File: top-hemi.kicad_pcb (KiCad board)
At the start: 2 copper layers, 46 x 39 mm, 37 parts, among them J1 USB_B_Mini, J2 TC2030_NL, J3 FFC-0.5MM-6POS, J4 Port_1, J5 Port_2, J6 FFC-0.5MM-6POS, J7 Port_3, J8 Port_4, U1 PMIC-LDO-XC6204B332MR_SOT23-5_, U2 LP2985-5.0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

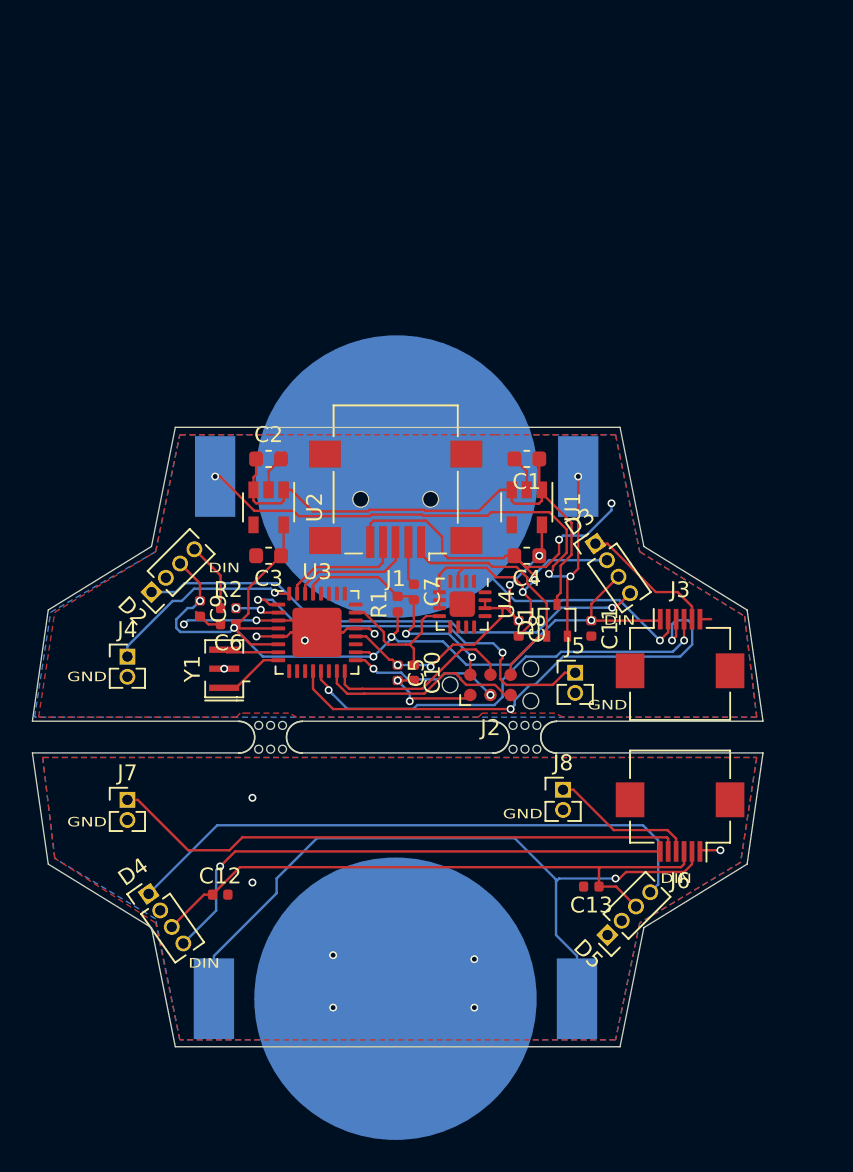
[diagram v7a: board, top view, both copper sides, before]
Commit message: Changed to 2.54mm
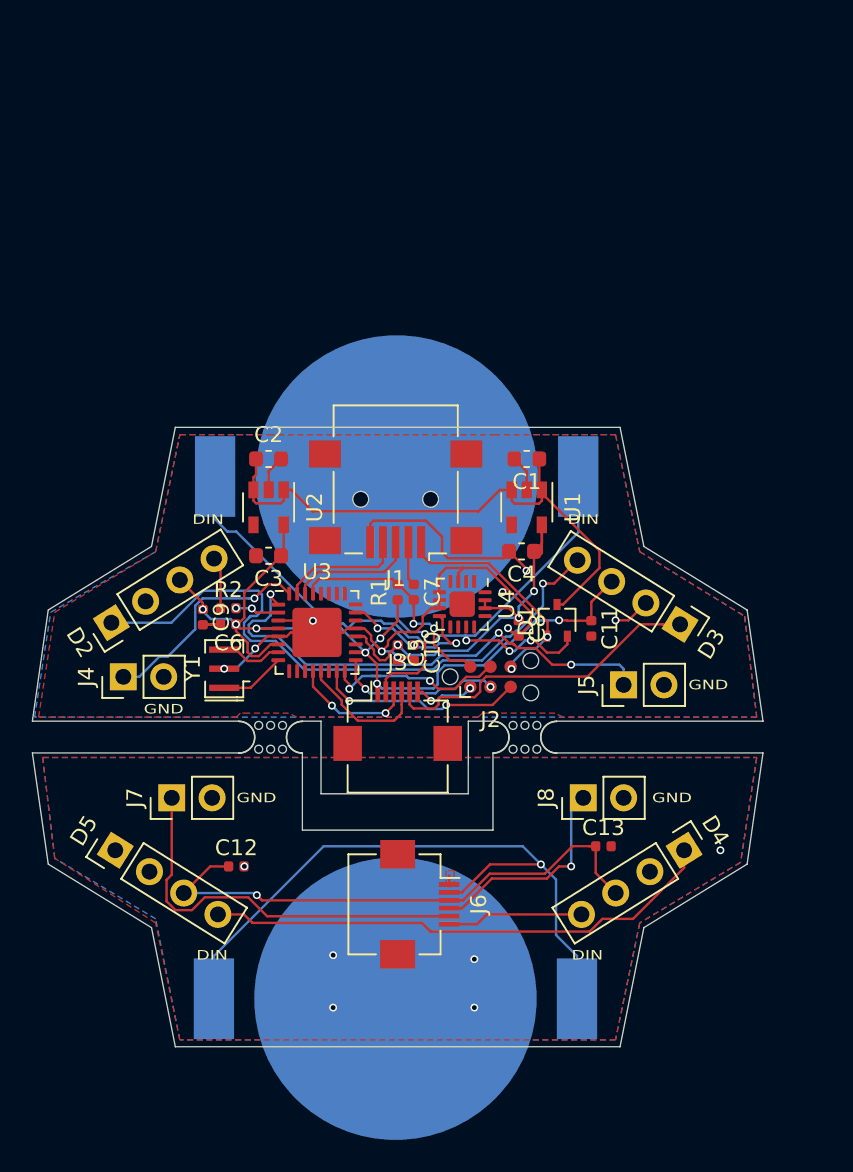
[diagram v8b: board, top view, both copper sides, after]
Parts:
- D2, D3, D4, D5: footprint Connector_PinHeader_1.27mm:PinHeader_1x04_P1.27mm_Vertical -> Connector_PinHeader_2.54mm:PinHeader_1x04_P2.54mm_Vertical
- J4, J5, J7, J8: footprint Connector_PinHeader_1.27mm:PinHeader_1x02_P1.27mm_Vertical -> Connector_PinHeader_2.54mm:PinHeader_1x02_P2.54mm_Vertical
- moved D4 33.8 mm to (151.1, 95.8), turned to 302 degrees
- moved D5 31.4 mm to (115.3, 95.8), turned to 58 degrees
- moved J3 18.4 mm to (133.1, 87.6)
- moved J6 17.2 mm to (134.5, 99.2), turned to 270 degrees
- moved D3 7.37 mm to (150.9, 81.5), turned to 238 degrees
- moved D2 3.18 mm to (115.1, 81.4), turned to 122 degrees
- moved J5 3.14 mm to (147.3, 85.3), turned to 90 degrees
- moved J7 2.80 mm to (118.9, 92.5), turned to 90 degrees
- moved C13 2.65 mm to (146.1, 95.5), turned to 0 degrees
- moved C12 2.05 mm to (122.9, 96.8)
- moved J8 1.37 mm to (144.8, 92.5), turned to 90 degrees
- moved J4 1.30 mm to (115.8, 84.8), turned to 90 degrees
- moved C10 1.27 mm to (134.1, 83.3)
- moved C5 1.27 mm to (133.1, 83.3)
- moved R1 0.76 mm to (133.1, 79.5)
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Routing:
- net /Bottom hemisphere/DIN-BOT: track 33.9 -> 8.58 mm, vias 1 -> 0
- net /Top Hemisphere/BNC-3: track 32.6 -> 7.79 mm
- net /Top Hemisphere/BNC-4: track 28.0 -> 8.39 mm, vias 2 -> 0
- net /Top Hemisphere/DOUT-BOT: track 8.52 -> 20.7 mm
- net GND: track 73.5 -> 61.4 mm, vias 19 -> 17
- net /Bottom hemisphere/BNC-3: track 36.5 -> 25.5 mm
- net +5V: track 98.9 -> 88.9 mm, vias 5 -> 8
- net /Top Hemisphere/BNC-2: track 25.1 -> 31.5 mm, vias 2 -> 3
- net Net-(D2-Pad1): track 33.1 -> 39.3 mm
- net /Top Hemisphere/BATT-BOT: track 28.8 -> 22.9 mm
- net Net-(D4-Pad1): track 37.7 -> 32.6 mm
- net /Top Hemisphere/BATT: track 38.8 -> 43.9 mm, vias 4 -> 3
- net /Bottom hemisphere/BATT-BOT: track 46.8 -> 42.5 mm
- net /Bottom hemisphere/BNC-4: track 9.19 -> 13.4 mm, vias 0 -> 1
- net +3V3: track 21.5 -> 24.3 mm, vias 5 -> 3
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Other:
- outline, holes or cut-outs redrawn
